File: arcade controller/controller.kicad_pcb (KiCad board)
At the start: 2 copper layers, 203.5 x 152.2 mm, 21 parts, among them SW1 LEFT, SW10 SELECT, SW2 DOWN, SW3 RIGHT, SW4 UP, SW5 X, SW6 Y, SW7 A, SW8 B, SW9 START

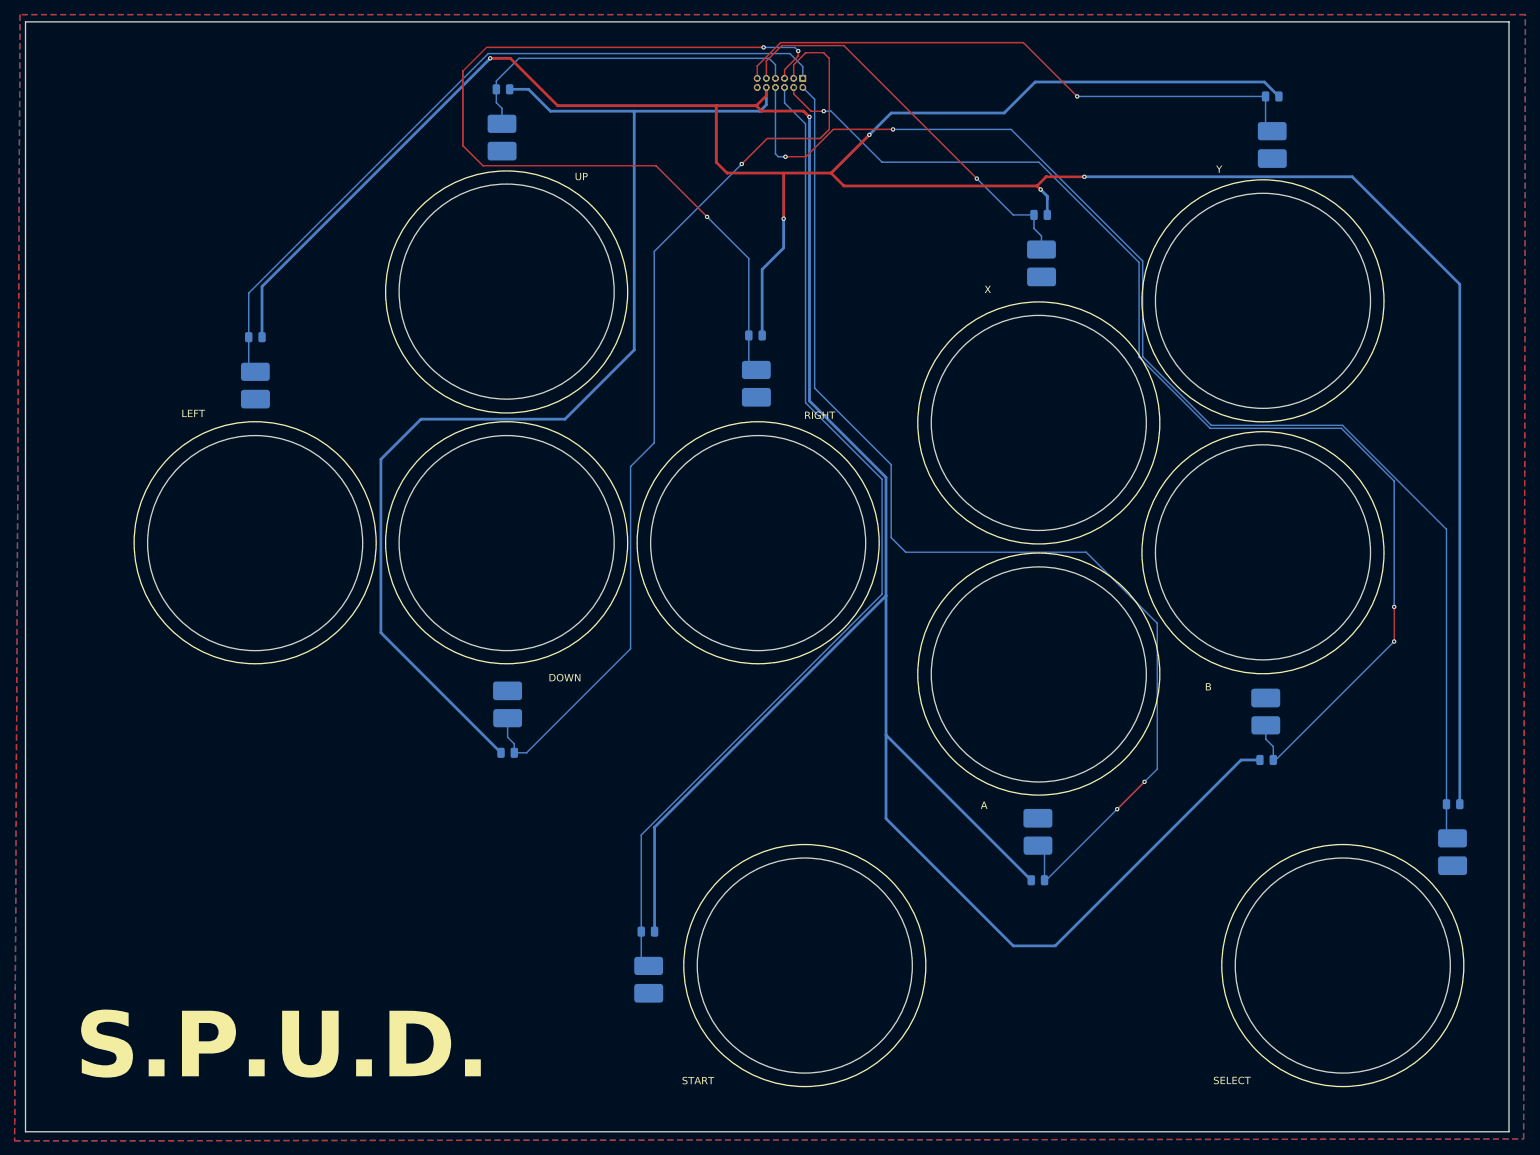
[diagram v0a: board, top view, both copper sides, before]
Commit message: updated controller with new connector
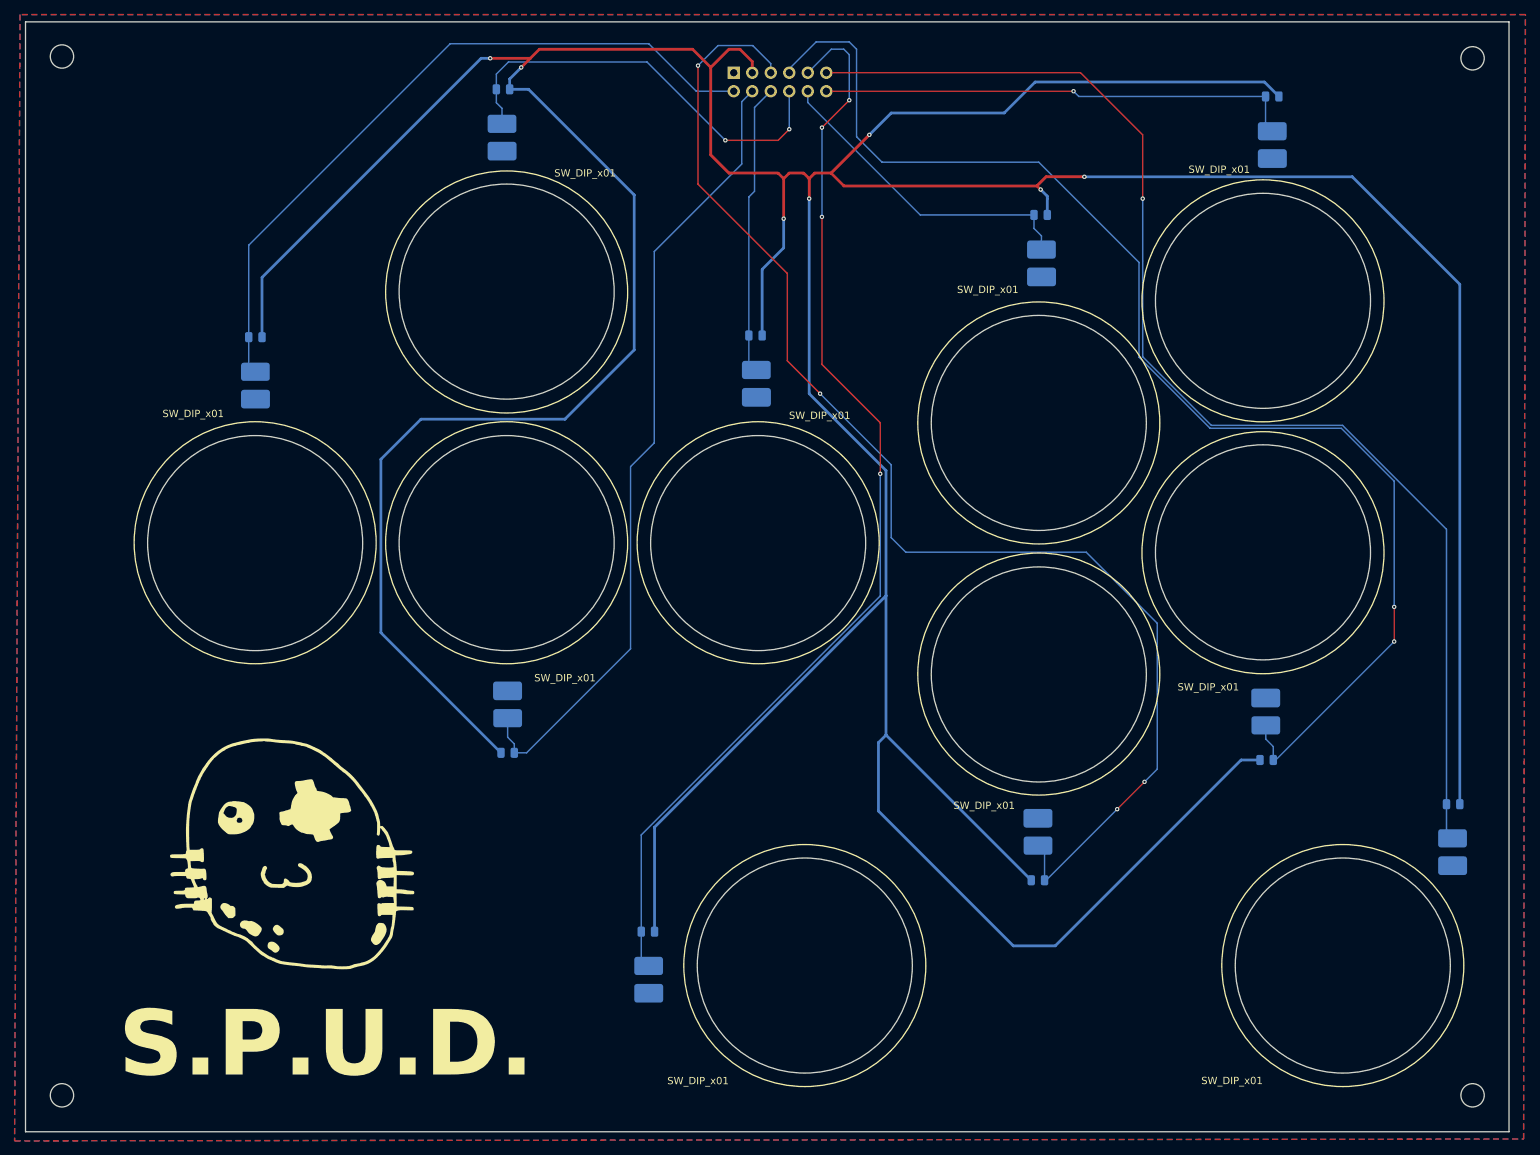
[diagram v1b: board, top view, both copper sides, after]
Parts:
- added G***: LOGO, spud real SMALL, F.Cu at (59.8, 132.5)
- added REF**: MountingHole_3.2mm_M3, MountingHole:MountingHole_3.2mm_M3, F.Cu at (26.5, 164.5)
- added REF**: MountingHole_3.2mm_M3, MountingHole:MountingHole_3.2mm_M3, F.Cu at (220.0, 22.2)
- added REF**: MountingHole_3.2mm_M3, MountingHole:MountingHole_3.2mm_M3, F.Cu at (220.0, 164.5)
- added REF**: MountingHole_3.2mm_M3, MountingHole:MountingHole_3.2mm_M3, F.Cu at (26.5, 22.0)
- ARCADE_PCB_CONN2: value Conn_02x06_Top_Bottom -> Conn_02x06_Odd_Even; footprint Connector_Harwin:Harwin_Gecko-G125-FVX1205L0X_2x06_P1.25mm_Vertical -> Connector_PinHeader_2.54mm:PinHeader_2x06_P2.54mm_Vertical
- SW1: value LEFT -> SW_DIP_x01
- SW10: value SELECT -> SW_DIP_x01
- SW2: value DOWN -> SW_DIP_x01
- SW3: value RIGHT -> SW_DIP_x01
- SW4: value UP -> SW_DIP_x01
- SW5: value X -> SW_DIP_x01
- SW6: value Y -> SW_DIP_x01
- SW7: value A -> SW_DIP_x01
- SW8: value B -> SW_DIP_x01
- SW9: value START -> SW_DIP_x01
- moved ARCADE_PCB_CONN2 9.51 mm to (118.7, 24.2), turned to -90 degrees
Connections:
- ARCADE_PCB_CONN2 pad 1: ARC1 -> GND
- ARCADE_PCB_CONN2 pad 10: ARC10 -> ARC5
- ARCADE_PCB_CONN2 pad 11: 3.3V -> ARC10
- ARCADE_PCB_CONN2 pad 12: GND -> ARC6
- ARCADE_PCB_CONN2 pad 2: ARC2 -> ARC1
- ARCADE_PCB_CONN2 pad 3: ARC3 -> 3.3V
- ARCADE_PCB_CONN2 pad 4: ARC4 -> ARC2
- ARCADE_PCB_CONN2 pad 5: ARC5 -> ARC7
- ARCADE_PCB_CONN2 pad 6: ARC6 -> ARC3
- ARCADE_PCB_CONN2 pad 7: ARC7 -> ARC8
- ARCADE_PCB_CONN2 pad 8: ARC8 -> ARC4
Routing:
- net ARC3: track 123.7 -> 39.9 mm, vias 3 -> 0
- net 3.3V: track 803.8 -> 770.5 mm, vias 6 -> 7
- net ARC7: track 155.0 -> 177.4 mm, vias 2 -> 4
- net ARC2: track 131.3 -> 110.4 mm, vias 1 -> 0
- net ARC6: track 81.0 -> 65.7 mm
- net ARC8: track 163.4 -> 175.1 mm, vias 3 -> 2
- net ARC9: track 140.1 -> 151.2 mm, vias 0 -> 4
- net ARC5: track 54.8 -> 44.1 mm, vias 1 -> 0
- net ARC4: track 48.4 -> 58.7 mm, vias 0 -> 2
- net ARC1: track 103.1 -> 98.4 mm
- net ARC10: track 176.3 -> 171.6 mm, vias 2 -> 1

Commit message: update arcade controller
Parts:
- ARCADE_PCB_CONN2: moved to F.Cu
- moved ARCADE_PCB_CONN2 12.7 mm to (131.3, 24.2)
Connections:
- ARCADE_PCB_CONN2 pad 1: GND -> ARC6
- ARCADE_PCB_CONN2 pad 10: ARC5 -> 3.3V
- ARCADE_PCB_CONN2 pad 11: ARC10 -> ARC1
- ARCADE_PCB_CONN2 pad 12: ARC6 -> GND
- ARCADE_PCB_CONN2 pad 2: ARC1 -> ARC10
- ARCADE_PCB_CONN2 pad 3: 3.3V -> ARC5
- ARCADE_PCB_CONN2 pad 4: ARC2 -> ARC9
- ARCADE_PCB_CONN2 pad 5: ARC7 -> ARC4
- ARCADE_PCB_CONN2 pad 6: ARC3 -> ARC8
- ARCADE_PCB_CONN2 pad 7: ARC8 -> ARC3
- ARCADE_PCB_CONN2 pad 8: ARC4 -> ARC7
- ARCADE_PCB_CONN2 pad 9: ARC9 -> ARC2
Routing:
- net ARC2: track 110.4 -> 274.2 mm
- net 3.3V: track 770.5 -> 808.0 mm, vias 7 -> 4
- net ARC7: track 177.4 -> 151.9 mm, vias 4 -> 2
- net ARC3: track 39.9 -> 61.0 mm, vias 0 -> 2
- net ARC10: track 171.6 -> 152.8 mm, vias 1 -> 2
- net ARC9: track 151.2 -> 138.3 mm, vias 4 -> 2
- net ARC8: track 175.1 -> 185.6 mm, vias 2 -> 0
- net ARC5: track 44.1 -> 53.3 mm
- net ARC4: track 58.7 -> 52.5 mm
- net ARC6: track 65.7 -> 69.6 mm, vias 1 -> 2
- net ARC1: track 98.4 -> 100.5 mm
